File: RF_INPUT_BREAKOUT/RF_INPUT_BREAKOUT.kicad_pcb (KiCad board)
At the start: 4 copper layers, 121 x 65 mm, 26 parts, among them IC1 SI4705-D62-GM, J5 Conn_2Rows-21Pins, U1 LD1117S33TR_SOT223, U2 LT5512EUF-PBF, X1 ASE-xxxMHz

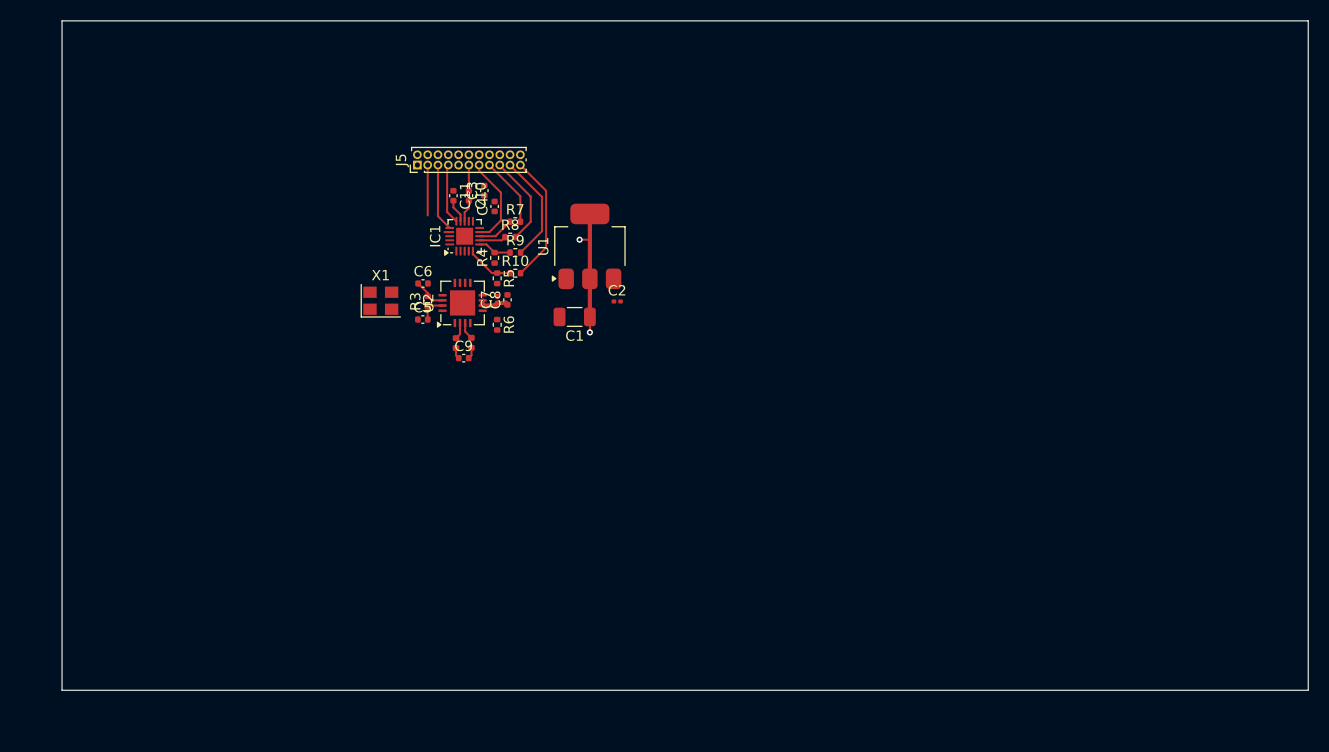
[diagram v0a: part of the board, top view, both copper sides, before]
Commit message: switched for LT5560 Mixer
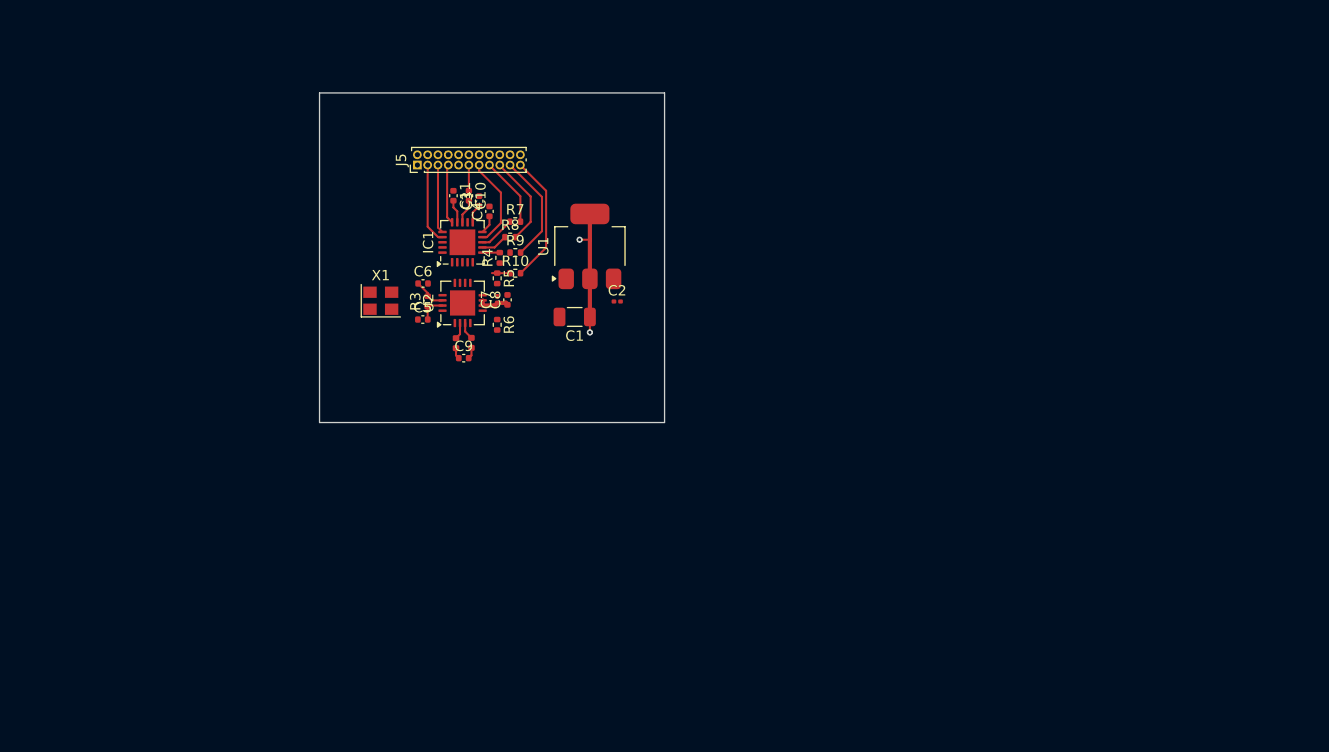
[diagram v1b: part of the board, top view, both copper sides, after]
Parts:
- IC1: footprint Package_DFN_QFN:QFN-20-1EP_3x3mm_P0.4mm_EP1.65x1.65mm -> Package_DFN_QFN:QFN-20-1EP_4x4mm_P0.5mm_EP2.5x2.5mm
- moved C3 1.14 mm to (127.5, 84.5)
- moved C4 0.69 mm to (128.5, 85.5)
- moved IC1 0.63 mm to (125.9, 88.5)
- moved R4 0.50 mm to (129.5, 90.0)
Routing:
- net +3.3V: track 12.5 -> 16.1 mm
- net /MCU_RF_RST: track 4.66 -> 1.76 mm
- net /RF_I2S_DCLK: track 5.42 -> 7.85 mm
- net /MCU_RF_SEN: track 3.29 -> 1.69 mm
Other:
- board size 121 x 65 mm -> 33.5 x 32 mm
